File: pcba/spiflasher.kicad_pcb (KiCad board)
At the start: 2 copper layers, 57.5 x 20.3 mm, 31 parts, among them J1 USB_B_Micro, J2 Conn_02x04_Counter_Clockwise, U1 TXB0104PW, U2 FT232H, Y1 12 MHz

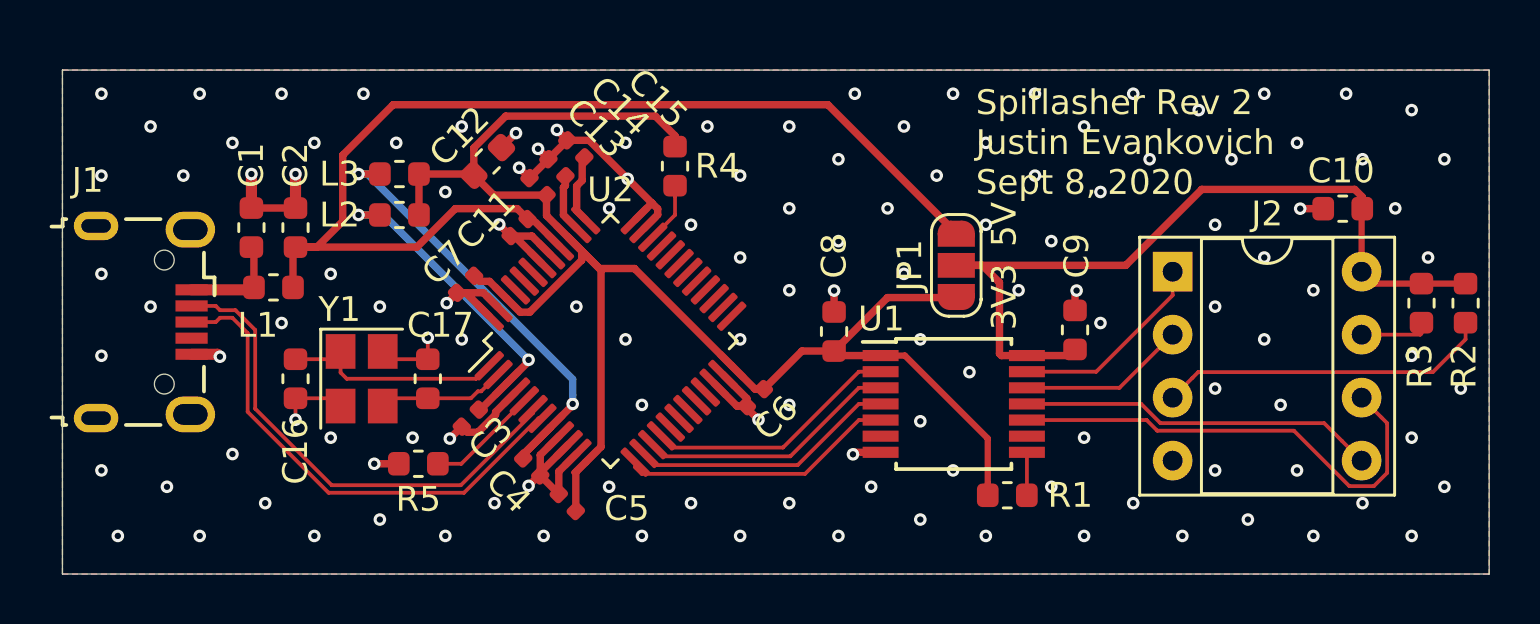
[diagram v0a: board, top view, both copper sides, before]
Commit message: Low profile USB port. Final Rev 2
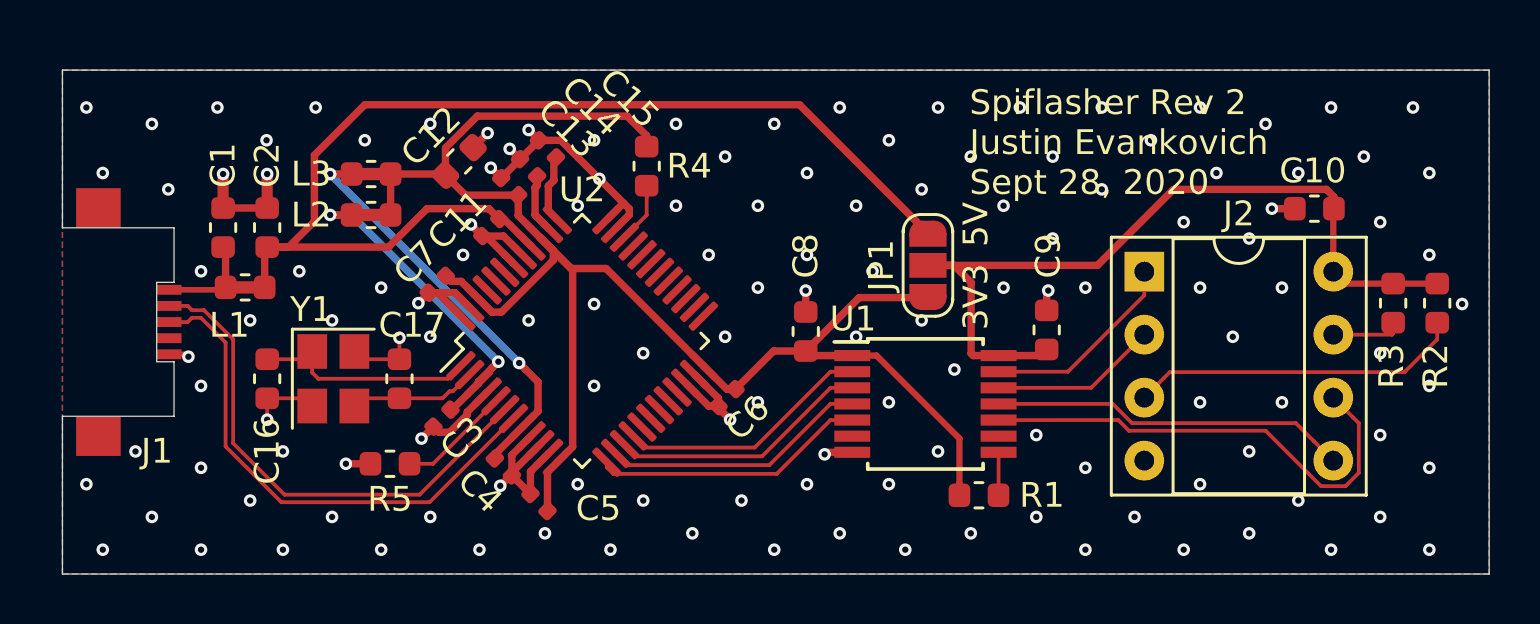
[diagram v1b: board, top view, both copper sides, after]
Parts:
- added NT1: Net-Tie_2, NetTie:NetTie-2_SMD_Pad0.5mm, F.Cu at (116.5, 100.2)
- added NT2: Net-Tie_2, NetTie:NetTie-2_SMD_Pad0.5mm, F.Cu at (121.5, 97.3)
- added NT3: Net-Tie_2, NetTie:NetTie-2_SMD_Pad0.5mm, F.Cu at (121.5, 95.6)
- J1: footprint Connector_USB:USB_Micro-B_Wuerth_629105150521 -> Local:USB_Micro-B_GCT_USB3070
- moved J1 1.51 mm to (110.9, 101.6)
- moved C13 1.14 mm to (127.1, 96.1)
- moved C14 1.14 mm to (127.9, 95.4)
- moved C1 1.14 mm to (115.6, 97.8)
- moved C10 1.14 mm to (159.6, 97.0)
- moved C11 1.14 mm to (126.4, 97.8)
- moved C12 1.14 mm to (125.1, 95.1)
- moved C15 1.14 mm to (128.7, 94.6)
- moved C16 1.14 mm to (117.3, 103.9)
- moved C17 1.14 mm to (122.7, 103.9)
- moved C2 1.14 mm to (117.3, 97.8)
- moved C3 1.14 mm to (124.4, 105.5)
- moved C5 1.14 mm to (128.3, 108.9)
- moved C6 1.14 mm to (135.9, 104.6)
- moved C7 1.14 mm to (124.2, 100.1)
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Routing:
- net Net-(C4-Pad1): track 18.5 -> 16.5 mm
- net /USB_D+: track 20.2 -> 20.9 mm
- net /USB_D-: track 20.0 -> 20.6 mm
- net GND: track 51.1 -> 50.8 mm, vias 130 -> 135
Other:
- outline, holes or cut-outs redrawn
- board text added: "Spiflasher Rev 2 Justin Evankovich Sept 28, 2020"
- board text removed: "Spiflasher Rev 2 Justin Evankovich Sept 8, 2020"
